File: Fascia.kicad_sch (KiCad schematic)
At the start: 94 parts, among them J1 Verdin iMX95, J2 Power in, J3 CAN to ECU, J4 Panel LVDS (provisional), J5 Pre-outs to amp, J6 Mic, Q1 NFET diode, Q2 NFET pass, Q3 NFET i2c xlat, Q4 NFET i2c xlat, U1 LM74930-Q1, U2 LM61460-Q1, U3 TLV767-Q1, U4 TCAN1044V-Q1, U5 SN65DSI85-Q1, U6 TLV767-Q1 3V3, U7 SN74AXC4T245-Q1, U8 SN74AXC4T245-Q1, U9 PCM3168A-Q1

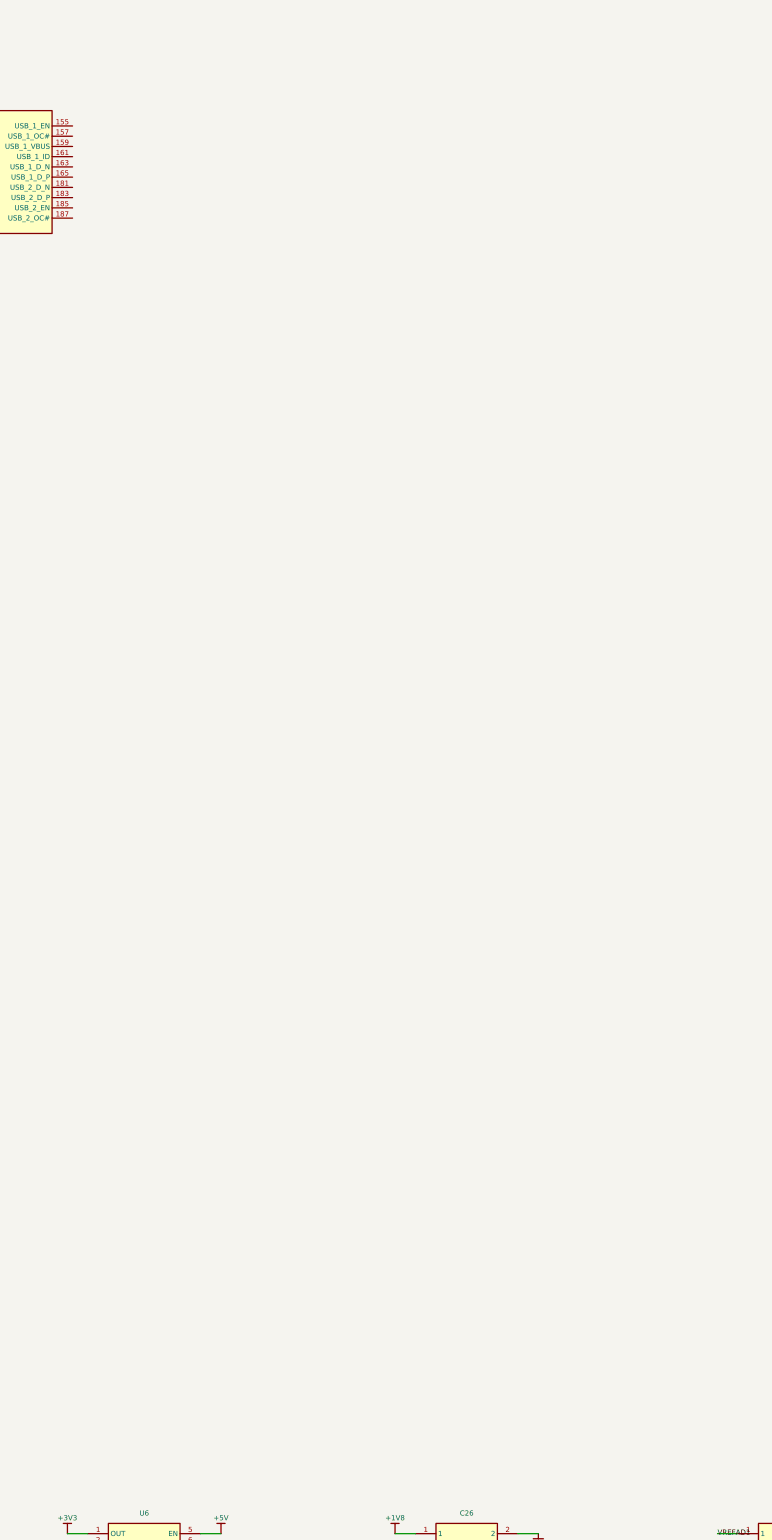
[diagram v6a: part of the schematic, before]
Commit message: Wire the USB-C port; catch a second silent net merge
Adds the USB-C port for wired CarPlay / Android Auto. ERC 35 -> 29, and
bank D is down to the panel touch link and the second CAN.

TPS2557-Q1 switches VBUS with a ~3.3 A limit, leaving margin over the
3 A advertised by the Rp resistors on CC1 and CC2. Both CC pins are
populated because Type-C is reversible. ID is strapped low for host
mode, VBUS sense is divided down to stay inside 1.8 V logic, and every
externally exposed pin gets ESD. No PD controller and no negotiation
firmware - Rp resistors are all a phone needs to charge at 15 W.

Two datasheet details worth recording, both in parts.py:

- EN polarity is the ONLY difference between the TPS2557-Q1 and the
  otherwise identical TPS2556-Q1: active high versus active low. Order
  the wrong one and the port is powered exactly when it should not be.
- VIH on EN is 1.1 V, so unlike the audio codec this path needs no level
  shifting - the module's 1.8 V GPIO drives it directly. FAULT is pulled
  to 1.8 V rather than the 5 V it switches, so it lands inside the
  module's input rating.

Also fixed: OUT1/OUT2 were both typed power_out, which made ERC report a
power-output conflict against what is physically one internal node
brought out on two pins to share current. Only one is a driver now.

The bigger fix is to the net-collision check. It caught its second real
merge - the USB block's USB_ILIM stub landing on connector unit D's
USB1_VBUS_SENSE stub - but only after being rewritten. The first version
scanned label positions and would have missed this entirely, because the
collision was between two stub ENDPOINTS, not two labels. It now records
every terminated coordinate, pin positions and stub endpoints alike, for
generic parts and the X1 connector both, and names both nets and both
owning references when they clash. Two silent merges in one session is
enough evidence that this check has to be structural rather than
incidental.

Co-Authored-By: Claude Opus 5 <norep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
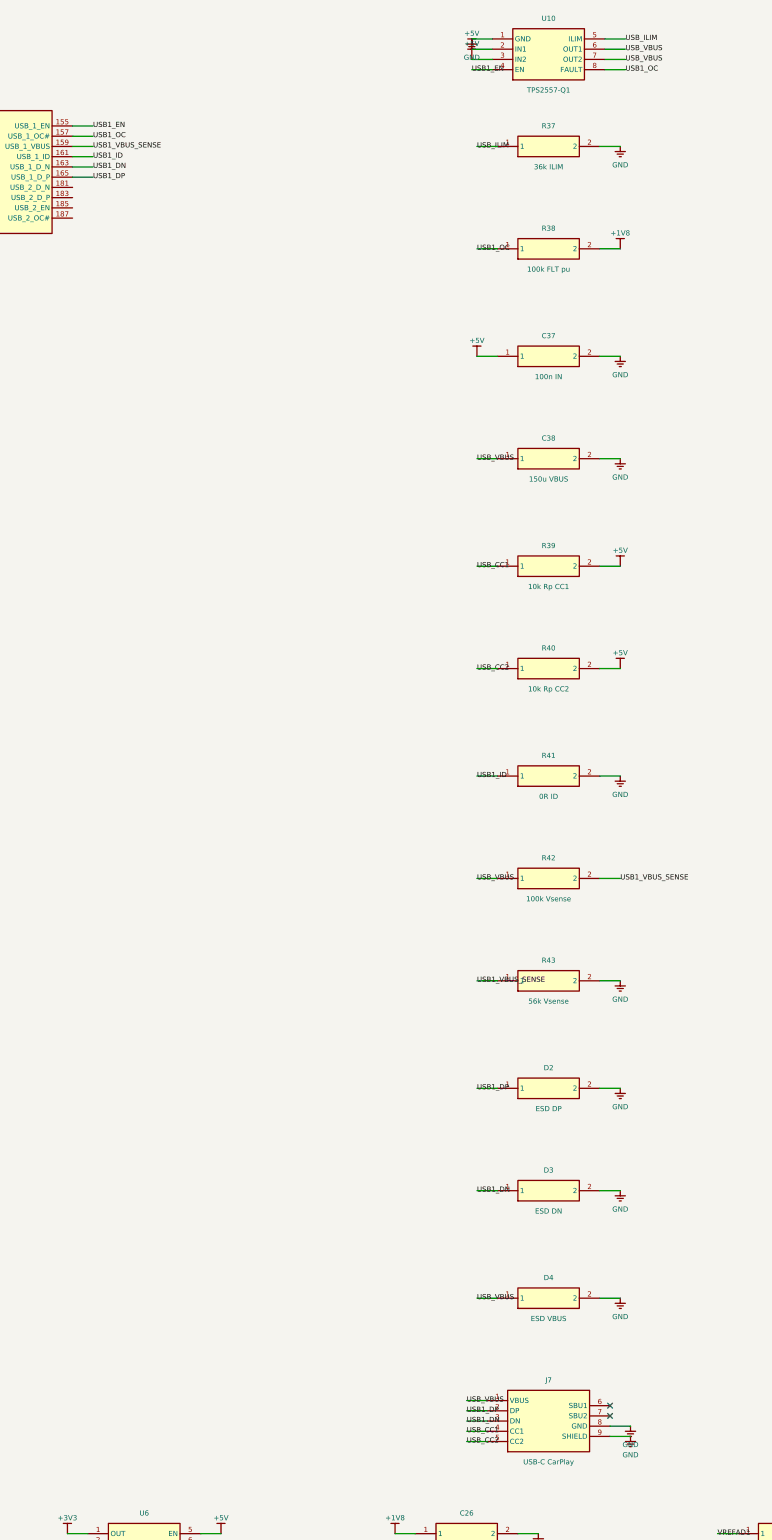
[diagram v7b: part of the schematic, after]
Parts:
- added C37: 100n IN, symbol Fascia:C
- added C38: 150u VBUS, symbol Fascia:C
- added D2: ESD DP, symbol Fascia:TVS
- added D3: ESD DN, symbol Fascia:TVS
- added D4: ESD VBUS, symbol Fascia:TVS
- added J7: USB-C CarPlay, symbol Fascia:CONN_USBC
- added R37: 36k ILIM, symbol Fascia:R
- added R38: 100k FLT pu, symbol Fascia:R
- added R39: 10k Rp CC1, symbol Fascia:R
- added R40: 10k Rp CC2, symbol Fascia:R
- added R41: 0R ID, symbol Fascia:R
- added R42: 100k Vsense, symbol Fascia:R
- added R43: 56k Vsense, symbol Fascia:R
- added U10: TPS2557-Q1, symbol Fascia:TPS2557-Q1
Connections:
- net +1V8: now also R38.2
- net +5V: now also C37.1, R39.2, R40.2, U10.2 (IN1), U10.3 (IN2)
- net GND: now also C37.2, C38.2, D2.2, D3.2, D4.2, J7.8 (GND), J7.9 (SHIELD), R37.2, R41.2, R43.2, U10.1 (GND)
- net USB1_EN: now reaches J1.155 (USB_1_EN)
- net USB1_EN: now also U10.4 (EN)
- net USB1_OC: now reaches J1.157 (USB_1_OC#)
- net USB1_OC: now also R38.1, U10.8 (FAULT)
- net USB1_VBUS_SENSE: now reaches J1.159 (USB_1_VBUS)
- net USB1_VBUS_SENSE: now also R42.2, R43.1
- net USB1_ID: now reaches J1.161 (USB_1_ID)
- net USB1_ID: now also R41.1
- net USB1_DN: now reaches J1.163 (USB_1_D_N)
- net USB1_DN: now also D3.1, J7.3 (DN)
- net USB1_DP: now reaches J1.165 (USB_1_D_P)
- net USB1_DP: now also D2.1, J7.2 (DP)
- new net USB_CC1: J7.4 (CC1), R39.1
- new net USB_CC2: J7.5 (CC2), R40.1
- new net USB_ILIM: R37.1, U10.5 (ILIM)
- new net USB_VBUS: C38.1, D4.1, J7.1 (VBUS), R42.1, U10.6 (OUT1), U10.7 (OUT2)
- no-connect marks 198 -> 200

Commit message: Wire control, sequencing and RTC backup; ERC down to 10 blocked items
Adds the JTAG header, power/recovery/reset buttons and the RTC coin
cell, and completes bank B. ERC 29 -> 10, and every remaining finding is
either blocked on a datasheet that has not arrived or deliberately
optional:

  2  PWM_3_DSI, GPIO_10_DSI   backlight, needs the iFan string V/I
  4  USB_2_*                  panel touch link, needs the touch
                              interface confirmed
  2  CAN_2_*                  optional second bus, no consumer chosen
  1  DSI_IRQ                  bridge interrupt, wants a spare GPIO
  1  IGN_SENSE                ignition sense, wants a module ADC

160 pins now carry real NoConnect items and 40 signal nets are wired.

The connection worth calling out is CTRL_PWR_EN_MOCI. It is the module's
own "carrier peripherals may power up now" output and stays high through
sleep, so it now gates the 1.8 V and 3.3 V LDOs instead of their being
tied permanently on. The carrier rails follow the module rather than
racing it at power-on.

RTC backup goes through a 47k series resistor because the Verdin
datasheet is explicit that anything lower can prevent the module
booting - an unusual failure mode to debug if it were missed.

Adds an X1_NC set for pins this board deliberately does not use that sit
outside the unused bank - CTRL_FORCE_OFF_MOCI#, CTRL_WAKE1_MICO# and
CTRL_SLEEP_MOCI# (all of which the datasheet permits floating), the two
TAMPER pins, PWR_1V8_MOCI (the carrier makes its own 1.8 V) and
PMIC_PGOOD. They get real NoConnect items rather than being left to
surface as ERC noise, so the remaining count means something.

Co-Authored-By: Claude Opus 5 <noreply@anthropic.com>
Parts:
- added C39: 100n, symbol Fascia:C
- added J10: RTC coin cell, symbol Fascia:CONN_CELL
- added J8: JTAG debug, symbol Fascia:CONN_JTAG
- added J9: Buttons, symbol Fascia:CONN_BTN
- added R44, R45, R46, R47: 10k pullup, symbol Fascia:R
- added R48: 10k JTAG Vref, symbol Fascia:R
- added R49: 47k min, symbol Fascia:R
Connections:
- net +1V8: now also R44.2, R45.2, R46.2, R47.2, R48.2
- net +5V: no longer U3.5 (EN), U6.5 (EN)
- net GND: now also C39.2, J10.2 (GND), J8.8 (GND), J9.4 (GND)
- net VBACKUP: now reaches J1.249 (VCC_BACKUP)
- net VBACKUP: now also C39.1, R49.2
- net JTAG_TDI: now reaches J1.1 (JTAG_1_TDI)
- net JTAG_TDI: now also J8.5 (TDI)
- net JTAG_TMS: now reaches J1.13 (JTAG_1_TMS)
- net JTAG_TMS: now also J8.2 (TMS)
- net RECOVERY: now reaches J1.246 (CTRL_RECOVERY_MICO#)
- net RECOVERY: now also J9.2 (RECOVERY), R45.1
- net PWR_BTN: now reaches J1.248 (CTRL_PWR_BTN_MICO#)
- net PWR_BTN: now also J9.1 (PWR_BTN), R44.1
- net PWR_EN_MOCI: now reaches J1.254 (CTRL_PWR_EN_MOCI)
- net PWR_EN_MOCI: now also U3.5 (EN), U6.5 (EN)
- net RESET_MOCI: now reaches J1.258 (CTRL_RESET_MOCI#)
- net RESET_MOCI: now also R47.1
- net RESET_MICO: now reaches J1.260 (CTRL_RESET_MICO#)
- net RESET_MICO: now also J8.7 (RESET), J9.3 (RESET), R46.1
- net JTAG_TRST: now reaches J1.3 (JTAG_1_TRST#)
- net JTAG_TRST: now also J8.6 (TRST)
- net JTAG_TDO: now reaches J1.5 (JTAG_1_TDO)
- net JTAG_TDO: now also J8.4 (TDO)
- net JTAG_VREF: now reaches J1.7 (JTAG_1_VREF)
- net JTAG_VREF: now also J8.1 (VREF), R48.1
- net JTAG_TCK: now reaches J1.9 (JTAG_1_TCK)
- net JTAG_TCK: now also J8.3 (TCK)
- new net VBACKUP_CELL: J10.1 (VBAT), R49.1
- no-connect marks 200 -> 207
